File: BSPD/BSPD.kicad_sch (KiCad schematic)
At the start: 61 parts, among them J1 DT13-48PABCD-R015, K1 Latching Relay, K2 Latching Relay, Q2 STS6NF20V, Q3 STS6NF20V, Q4 STS6NF20V, U1 LM7805CT, U10 DK1A1B-12V, U12 LM555N, U13 LM7805CT, U14 ISO1050DUB, U15 LM7809_TO220, U17 NAND, U2 NSL-32, U2 OP AMP, U3 OP AMP, U4 NUCLEO-L432KC, U5 2x4 OR GATE, U6 LM555N, U8 NAND, U9 AND GATE

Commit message: cleared acc stuff
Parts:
- removed C17, C8: 100nf, Capacitor_SMD:C_0805_2012Metric_Pad1.18x1.45mm_HandSolder, symbol Device:C
- removed C4: 1uf, Capacitor_SMD:C_0805_2012Metric_Pad1.18x1.45mm_HandSolder, symbol Device:C
- removed C7: 330nf, Capacitor_SMD:C_0805_2012Metric_Pad1.18x1.45mm_HandSolder, symbol Device:C
- removed D4, D5: D, Diode_SMD:D_2010_5025Metric_Pad1.52x2.65mm_HandSolder, symbol Device:D
- removed K2: Latching Relay, 1FS_2_Global_Footprint_Library:Omron G6BK-1114P-US, symbol 1_Personal_FS_Library:G6BK-1114P-US
- removed Q4: STS6NF20V, 1FS_2_Global_Footprint_Library:SO-8_STM, symbol 1_ACC_BOARD:STS6NF20V
- removed R13: 374, Resistor_SMD:R_0805_2012Metric_Pad1.20x1.40mm_HandSolder, symbol Device:R_US
- removed R17: 2.4M, Resistor_SMD:R_0805_2012Metric_Pad1.20x1.40mm_HandSolder, symbol Device:R_US
- removed U12: LM555N, Package_DIP:DIP-8_W7.62mm, symbol 2FS-1_Symbol Library:LM555N
- removed U13: LM7805CT, Package_TO_SOT_THT:TO-220-3_Vertical, symbol Regulator_Linear:LM317_TO-252
- removed U17: NAND, Package_DIP:DIP-14_W7.62mm, symbol 4xxx:4023
- removed U?: NSL-32, 1FS_2_Global_Footprint_Library:OptoCoupler 6-SOP, symbol Isolator:NSL-32
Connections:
- no-connect marks 46 -> 44
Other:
- note removed: "8-12V"
- note removed: "~3.5 sec 555 delay before turn on"

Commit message: Schematic implementation of current differential circuit
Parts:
- added R13, R16: 39k, Resistor_SMD:R_0805_2012Metric_Pad1.20x1.40mm_HandSolder, symbol Device:R_US
- added R17, R18: 1M, Resistor_SMD:R_0805_2012Metric_Pad1.20x1.40mm_HandSolder, symbol Device:R_US
- added R19: 22k 1%, Resistor_SMD:R_0805_2012Metric_Pad1.20x1.40mm_HandSolder, symbol Device:R_US
- added R20: 18k 1%, Resistor_SMD:R_0805_2012Metric_Pad1.20x1.40mm_HandSolder, symbol Device:R_US
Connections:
- net +5V: now also R19.2
- net Current Output: now also R13.2; no longer U2.3
- net Current Vref: now also R16.1; no longer U2.2
- net GND: now also R18.2, R20.2
- net Current Vref Op: now reaches U3.5
- net Current Vref Op: now also R16.2, R17.2
- net Current Output Op: now reaches U3.6
- net Current Output Op: now also R13.1, R18.1
- net Current Sensor Differential: now reaches U3.7
- net Current Sensor Differential: now also U2.3, R17.1
- new net 2.25V: R19.1, R20.1, U2.2
- no-connect marks 44 -> 41
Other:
- note added: "Corresponds to 2.588 V from current sensor or .088 diff Shown both in testing and falstad. Will require further testing once complete (r values)"
- note added: "~ 250 Gain 0.2V -> 5V"
- moved on the sheet: C11, C12, C13, C14, C15, C16, C3, D1, D2, D3, K1, R14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

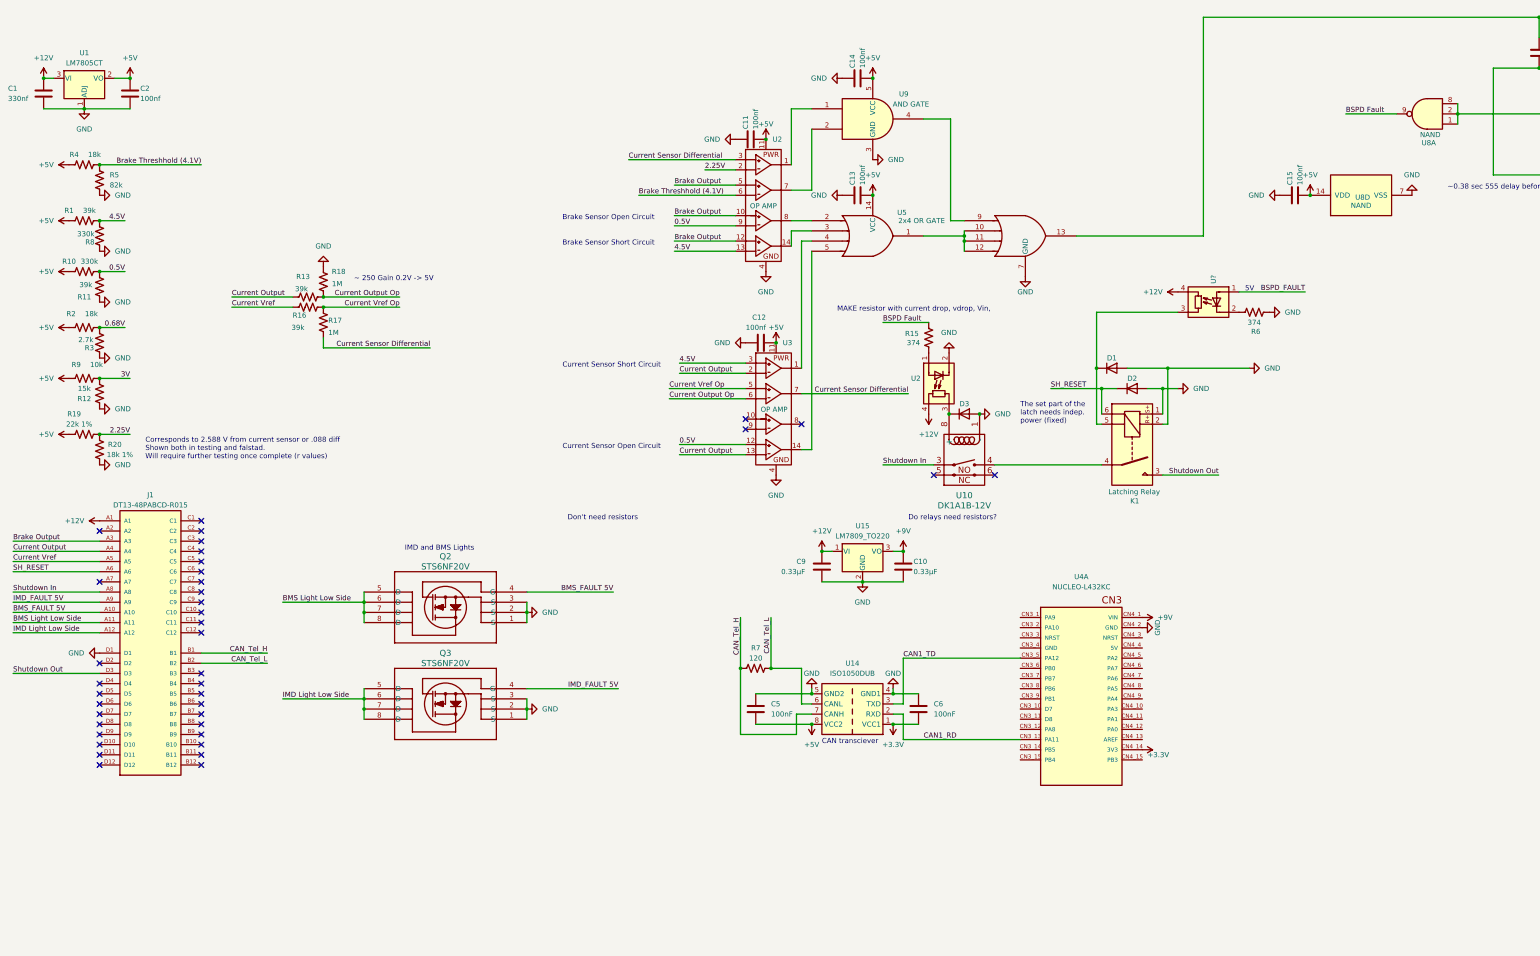
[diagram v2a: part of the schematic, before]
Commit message: Compartmentalized some parts of board in diagram
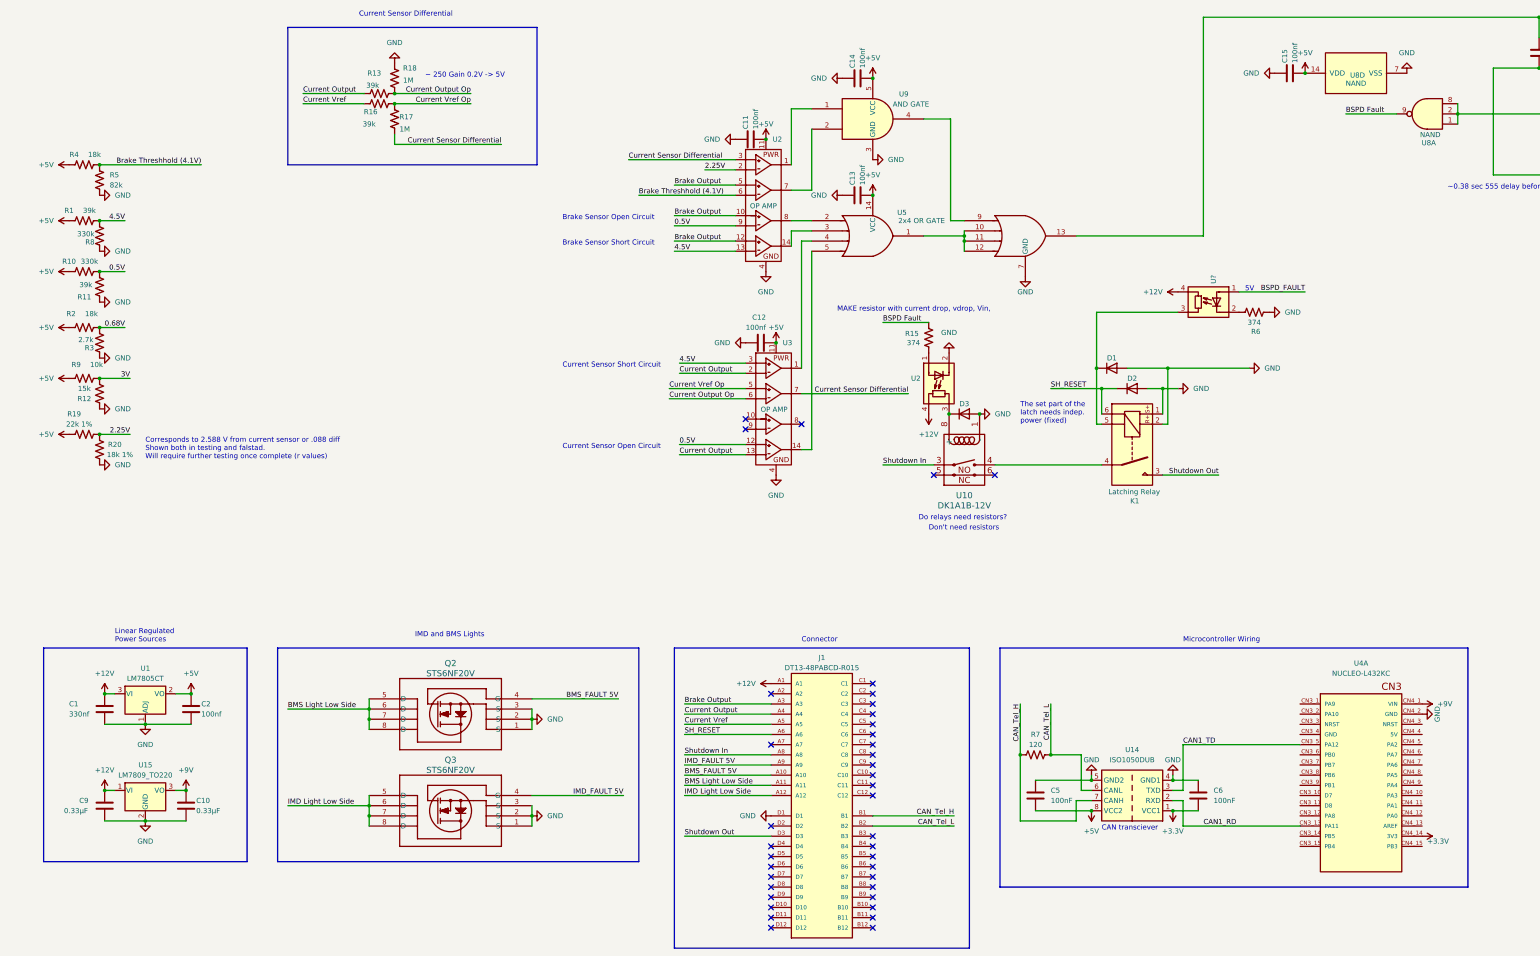
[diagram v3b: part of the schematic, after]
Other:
- note added: "Connector"
- note added: "Current Sensor Differential"
- note added: "Linear Regulated Power Sources"
- note added: "Microcontroller Wiring"
- moved on the sheet: C1, C10, C15, C2, C5, C6, C9, J1, Q2, Q3, R13, R16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

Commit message: Finished compartmentalization and buffering
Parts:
- added C4: 100nf, Capacitor_SMD:C_0805_2012Metric_Pad1.18x1.45mm_HandSolder, symbol Device:C
- added U12: OP AMP, Package_DIP:DIP-14_W7.62mm, symbol 1_Personal_FS_Library:4_Set_OpAmp
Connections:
- net +5V: now also C4.2, U12.11
- net BSPD Fault: now also C3.1, U5.13, U6.4 (R); no longer R15.2, U8.9
- net Current Output: now also U3.10; no longer R13.2
- net Current Vref: now also U12.3; no longer R16.1
- net GND: now also C4.1, U12.4
- net Current Output Buffered: now reaches U3.8
- net Current Output Buffered: now also R13.2, U3.9
- net BSPD_FAULT renamed BSPD Fault Post Timer
- net BSPD Fault Post Timer: now also R15.2, U8.9
- new net Current Vref Buffered: R16.1, U12.1, U12.2
- no-connect marks 41 -> 47
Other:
- note added: "BPSD Timer"
- note added: "Current Sensor Buffering"
- note added: "Main BSPD Comparison"
- note added: "OpAmp BSPD Logic"
- note added: "Shutdown Control"
- note added: "Voltage Dividers"
- moved on the sheet: C1, C10, C11, C12, C13, C14, C15, C16, C2, C3, C5, C6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

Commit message: 1/2 BSPD Circuitry
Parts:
- removed R2: 18k, Resistor_SMD:R_0805_2012Metric_Pad1.20x1.40mm_HandSolder, symbol Device:R_US
- removed R3: 2.7k, Resistor_SMD:R_0805_2012Metric_Pad1.20x1.40mm_HandSolder, symbol Device:R_US
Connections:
- net BMS Light Low Side: now also J1.D10; no longer J1.A11
- net BMS_FAULT 5V: now also J1.D9; no longer J1.A10
- net CAN_Tel_L: now also J1.B12; no longer J1.B2
- net IMD Light Low Side: now also J1.D11; no longer J1.A12
- net IMD_FAULT 5V: now also J1.D8; no longer J1.A9
- net SH_RESET: now also J1.D7; no longer J1.A6
- net Shutdown In: now also J1.A2; no longer J1.A8
- net Shutdown Out: now also J1.D12; no longer J1.D3
- net CurSenShort: now reaches U3.1, U5.4
- net CurSenOpen: now reaches U3.14, U5.5
- net BrkSenOpen: now reaches U2.8, U5.2
- net BrkSenShort: now reaches U2.14, U5.3
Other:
- title: Brake System Plausability Device -> Brake System Plausability Device +
- moved on the sheet: R1, R10, R11, R12, R19, R20, R4, R5, R8, R9

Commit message: Silk screen complete
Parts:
- R15, R6: value 374 -> 370
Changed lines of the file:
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@@
       (effects (font (size 1.27 1.27)))
     )
-    (property "Value" "374" (at 494.03 39.37 90)
+    (property "Value" "370" (at 494.03 39.37 90)
       (effects (font (size 1.27 1.27)))
     )
@@
       (effects (font (size 1.27 1.27)))
     )
-    (property "Value" "374" (at 407.67 38.1 0)
-      (effects (font (size 1.27 1.27)))
-    )
+    (property "Value" "370" (at 407.67 38.1 0)
+      (effects (font (size 1.27 1.27)))
+    )

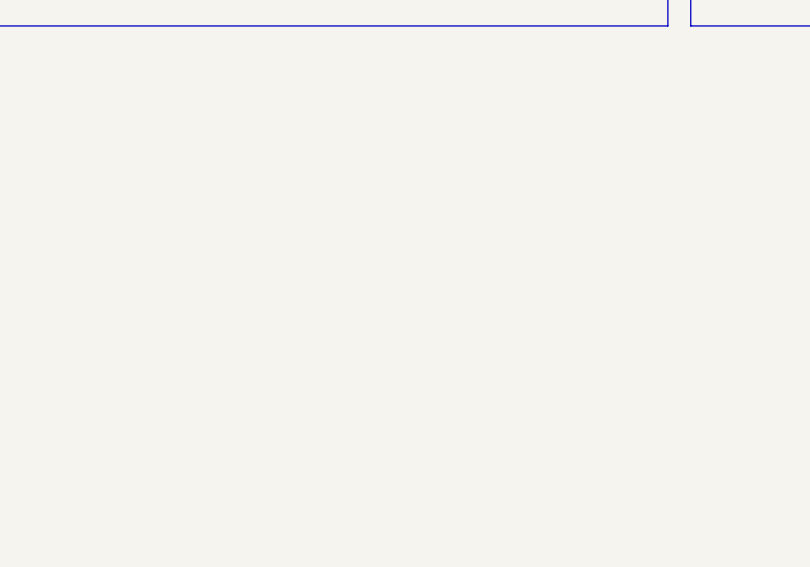
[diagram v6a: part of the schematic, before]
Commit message: Moved default kicad models to folder and finished 3d models for board
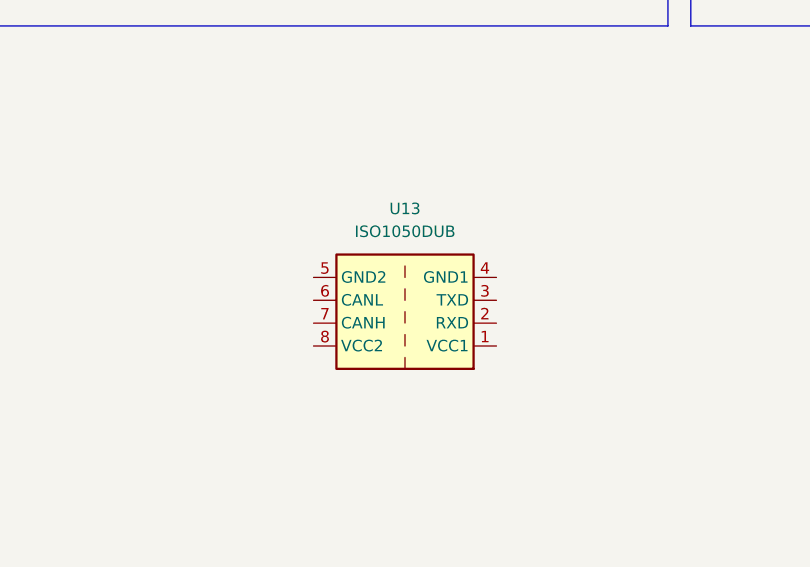
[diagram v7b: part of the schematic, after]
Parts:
- added U13: ISO1050DUB, Package_SO:SOP-8_6.62x9.15mm_P2.54mm, symbol Interface_CAN_LIN:ISO1050DUB
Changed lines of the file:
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@@
+    )
+  )
+  (symbol (lib_id "Interface_CAN_LIN:ISO1050DUB") (at 81.28 182.88 180) (unit 1)
+    (in_bom yes) (on_board yes) (dnp no) (fields_autoplaced)
+    (property "Reference" "U13" (at 81.28 170.18 0)
+      (effects (font (size 1.27 1.27)))
+    )
+    (property "Value" "ISO1050DUB" (at 81.28 172.72 0)
+      (effects (font (size 1.27 1.27)))
+    )
+    (property "Footprint" "Package_SO:SOP-8_6.62x9.15mm_P2.54mm" (at 81.28 173.99 0)
+      (effects (font (size 1.27 1.27) italic) hide)
+    )
+    (property "Datasheet" "http://www.ti.com/lit/ds/symlink/iso1050.pdf" (at 81.28 181.61 0)
+      (effects (font (size 1.27 1.27)) hide)
+    )
+    (pin "1")
+    (pin "2")
+    (pin "3")
+    (pin "4")
+    (pin "5")
+    (pin "6")
+    (pin "7")
+    (pin "8")
+    (instances
+      (project "BSPD"
+        (path "/9b958334-fa88-4811-8197-71444a07b1b5"
+          (reference "U13") (unit 1)
+        )
+      )
+      (project "Acc_Board"
+        (path "/e19d26dd-723b-45e6-9d59-b1730158e759"
+          (reference "U1") (unit 1)
+        )
+      )
     )
   )

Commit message: Added logo + updated board date
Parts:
- removed U13: ISO1050DUB, Package_SO:SOP-8_6.62x9.15mm_P2.54mm, symbol Interface_CAN_LIN:ISO1050DUB
- added SYM1: SYM_EasterEgg_42x60mm, 1FS_2_Global_Footprint_Library:FORMULA SLUG, symbol Graphic:SYM_EasterEgg_42x60mm
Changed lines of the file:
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@@
+    )
+  )
+  (symbol (lib_id "Graphic:SYM_EasterEgg_42x60mm") (at 548.64 86.36 0) (unit 1)
+    (in_bom no) (on_board yes) (dnp no) (fields_autoplaced)
+    (property "Reference" "SYM1" (at 548.64 86.36 0)
+      (effects (font (size 1.27 1.27)) hide)
+    )
+    (property "Value" "SYM_EasterEgg_42x60mm" (at 548.64 86.36 0)
+      (effects (font (size 1.27 1.27)) hide)
+    )
+    (property "Footprint" "1FS_2_Global_Footprint_Library:FORMULA SLUG" (at 548.64 90.17 0)
+      (effects (font (size 1.27 1.27)) hide)
+    )
+    (property "Datasheet" "https://eur-lex.europa.eu/LexUriServ/LexUriServ.do?uri=OJ:L:2013:347:0671:0854:de:PDF" (at 548.64 92.71 0)
+      (effects (font (size 1.27 1.27)) hide)
+    )
+    (property "Sim.Enable" "0" (at 548.64 88.9 0)
+      (effects (font (size 1.27 1.27)) hide)
+    )
+    (instances
+      (project "BSPD"
+        (path "/9b958334-fa88-4811-8197-71444a07b1b5"
+          (reference "SYM1") (unit 1)
+        )
+      )
     )
   )
@@
         )
       )
-    )
-  )
-  (symbol (lib_id "Interface_CAN_LIN:ISO1050DUB") (at 81.28 182.88 180) (unit 1)
-    (in_bom yes) (on_board yes) (dnp no) (fields_autoplaced)
-    (property "Reference" "U13" (at 81.28 170.18 0)
-      (effects (font (size 1.27 1.27)))
-    )
-    (property "Value" "ISO1050DUB" (at 81.28 172.72 0)
-      (effects (font (size 1.27 1.27)))
-    )
-    (property "Footprint" "Package_SO:SOP-8_6.62x9.15mm_P2.54mm" (at 81.28 173.99 0)
-      (effects (font (size 1.27 1.27) italic) hide)
-    )
-    (property "Datasheet" "http://www.ti.com/lit/ds/symlink/iso1050.pdf" (at 81.28 181.61 0)
-      (effects (font (size 1.27 1.27)) hide)
-    )
-    (pin "1")
-    (pin "2")
-    (pin "3")
-    (pin "4")
-    (pin "5")
-    (pin "6")
-    (pin "7")
-    (pin "8")
-    (instances
-      (project "BSPD"
-        (path "/9b958334-fa88-4811-8197-71444a07b1b5"
-          (reference "U13") (unit 1)
-        )
-      )
-      (project "Acc_Board"
-        (path "/e19d26dd-723b-45e6-9d59-b1730158e759"
-          (reference "U1") (unit 1)
-        )
-      )
